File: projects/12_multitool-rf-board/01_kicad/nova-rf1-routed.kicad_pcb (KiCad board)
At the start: 4 copper layers, 110 x 66 mm, 87 parts, among them M1 vibro, SW1 RFswitch, SW2 RFswitch, U1 STM32WB55RG, U10 ESD, U2 CC1101, U3 ST25R3916, U5 ST7565R, U6 BQ25896, U7 BQ27220, U8 LM3281, U8B LM3281, U9 loadsw, X10 BAT+NTC, X6 FFC 18p, Y1 32MHz, Y2 32.768kHz

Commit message: proj12: rename board CRL-MT1 -> NOVA-RF1 (project-wide)
Global rename across source, docs, generated schematic/board/footprint-lib,
BOM/CPL, enclosure and fab tooling. No functional change. Footprint library
prefix crl-mt1: -> nova-rf1:; silkscreen/title/fab-file names updated.
(The in-flight compact route output will be renamed when it completes.)

Co-Authored-By: Claude Opus 4.8 <noreply@anthropic.com>
Claude-Session: https://claude.ai/code/session_01Hk6s8R6up8HYVQWXd3atVk
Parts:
- ANT1: footprint crl-mt1:Antenna_Chip -> nova-rf1:Antenna_Chip
- ANT_LF: footprint crl-mt1:RFID_125k_Coil -> nova-rf1:RFID_125k_Coil
- ANT_NFC: footprint crl-mt1:NFC_Loop_Antenna -> nova-rf1:NFC_Loop_Antenna
- BT1: footprint crl-mt1:Battery_3p -> nova-rf1:Battery_3p
- DA7: footprint crl-mt1:LP5562_DSBGA12 -> nova-rf1:LP5562_DSBGA12
- FLT1: footprint crl-mt1:RF_filter -> nova-rf1:RF_filter
- FLT2: footprint crl-mt1:Johanson_0310_Balun -> nova-rf1:Johanson_0310_Balun
- J_IBTN: footprint crl-mt1:iButton_Contacts -> nova-rf1:iButton_Contacts
- J_SD: footprint crl-mt1:microSD_7p -> nova-rf1:microSD_7p
- J_SWD: footprint crl-mt1:TagConnect_TC2030 -> nova-rf1:TagConnect_TC2030
- LS1: footprint crl-mt1:Speaker_2p -> nova-rf1:Speaker_2p
- M1: footprint crl-mt1:Vibro_2p -> nova-rf1:Vibro_2p
- SW1, SW2: footprint crl-mt1:RF_Switch_TSNP9 -> nova-rf1:RF_Switch_TSNP9
- U5: footprint crl-mt1:Display_ST7565_FFC -> nova-rf1:Display_ST7565_FFC
- U_IR: footprint crl-mt1:TSOP_IR_3p -> nova-rf1:TSOP_IR_3p
- VD4: footprint crl-mt1:LED_RGB_4p -> nova-rf1:LED_RGB_4p
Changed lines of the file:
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@@
 	(net 176 "unconnected-(U9-4)")
 	(net 177 "unconnected-(U9-5)")
-	(footprint "crl-mt1:TSOP_IR_3p"
+	(footprint "nova-rf1:TSOP_IR_3p"
 		(layer "F.Cu")
 		(at 66.065001 61.7751)
@@
 		(embedded_fonts no)
 	)
-	(footprint "crl-mt1:RF_Switch_TSNP9"
+	(footprint "nova-rf1:RF_Switch_TSNP9"
 		(layer "F.Cu")
 		(at 69.247619 71.9316)
@@
 		(embedded_fonts no)
 	)
-	(footprint "crl-mt1:Speaker_2p"
+	(footprint "nova-rf1:Speaker_2p"
 		(layer "F.Cu")
 		(at 99.617858 47.6786)
@@
 		(embedded_fonts no)
 	)
-	(footprint "crl-mt1:microSD_7p"
+	(footprint "nova-rf1:microSD_7p"
 		(layer "F.Cu")
 		(at 81.117858 47.2786)
@@
 		)
 	)
-	(footprint "crl-mt1:LP5562_DSBGA12"
+	(footprint "nova-rf1:LP5562_DSBGA12"
 		(layer "F.Cu")
 		(at 101.113334 71.088)
@@
 		)
 	)
-	(footprint "crl-mt1:LED_RGB_4p"
+	(footprint "nova-rf1:LED_RGB_4p"
 		(layer "F.Cu")
 		(at 82.466666 72.0316)
@@
 		)
 	)
-	(footprint "crl-mt1:Johanson_0310_Balun"
+	(footprint "nova-rf1:Johanson_0310_Balun"
 		(layer "F.Cu")
 		(at 106.117145 71.5316)
@@
 		(embedded_fonts no)
 	)
-	(footprint "crl-mt1:RF_filter"
+	(footprint "nova-rf1:RF_filter"
 		(layer "F.Cu")
 		(at 55.75 71.6316)
@@
 		(embedded_fonts no)
 	)
-	(footprint "crl-mt1:NFC_Loop_Antenna"
+	(footprint "nova-rf1:NFC_Loop_Antenna"
 		(locked yes)
 		(layer "F.Cu")
@@
 		(embedded_fonts no)
 	)
-	(footprint "crl-mt1:TagConnect_TC2030"
+	(footprint "nova-rf1:TagConnect_TC2030"
 		(locked yes)
 		(layer "F.Cu")
@@
 		)
 	)
-	(footprint "crl-mt1:iButton_Contacts"
+	(footprint "nova-rf1:iButton_Contacts"
 		(layer "F.Cu")
 		(at 90.367858 48.1786)
@@
 		)
 	)
-	(footprint "crl-mt1:Antenna_Chip"
+	(footprint "nova-rf1:Antenna_Chip"
 		(locked yes)
 		(layer "F.Cu")
@@
 		(embedded_fonts no)
 	)
-	(footprint "crl-mt1:Display_ST7565_FFC"
+	(footprint "nova-rf1:Display_ST7565_FFC"
 		(layer "F.Cu")
 		(at 57.675001 61.8751)
@@
 		)
 	)
-	(footprint "crl-mt1:RF_Switch_TSNP9"
+	(footprint "nova-rf1:RF_Switch_TSNP9"
 		(layer "F.Cu")
 		(at 75.866666 71.9316)
@@
 		)
 	)
-	(footprint "crl-mt1:RFID_125k_Coil"
+	(footprint "nova-rf1:RFID_125k_Coil"
 		(locked yes)
 		(layer "F.Cu")
@@
 		)
 	)
-	(footprint "crl-mt1:Vibro_2p"
+	(footprint "nova-rf1:Vibro_2p"
 		(layer "F.Cu")
 		(at 62.613096 72.6316)
@@
 		(embedded_fonts no)
 	)
-	(footprint "crl-mt1:Battery_3p"
+	(footprint "nova-rf1:Battery_3p"
 		(layer "F.Cu")
 		(at 90.574049 61.9751)

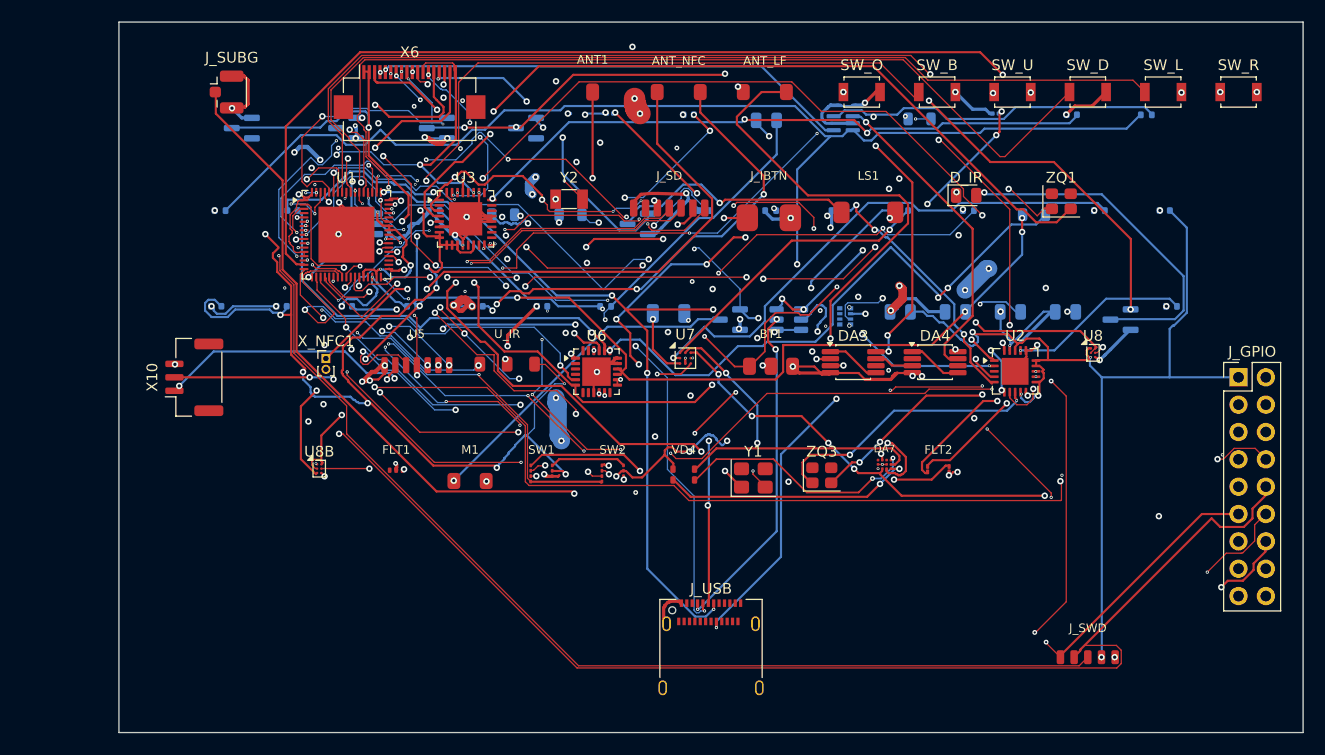
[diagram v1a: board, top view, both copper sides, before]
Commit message: proj12: NOVA-RF1 compact route 103/104 + both planes + full fab package
- +3V3 plane on In2.Cu (power nets closed), GND plane on In1.Cu
- 103/104 nets routed (NFC_CS needs 1 manual trace - only top+bottom free on a
  2-plane 4-layer board), 2965 segments, 530 vias; silkscreen added
- fab package: Gerber X2 + Excellon drill + map, CPL, JLCPCB + costed BOM
  (03_fab/NOVA-RF1_gerbers.zip etc.), names corrected in fab_export.sh
- refreshed routed-board render + product PDF; PCB_STATUS.md final section

Co-Authored-By: Claude Opus 4.8 <noreply@anthropic.com>
Claude-Session: https://claude.ai/code/session_01Hk6s8R6up8HYVQWXd3atVk
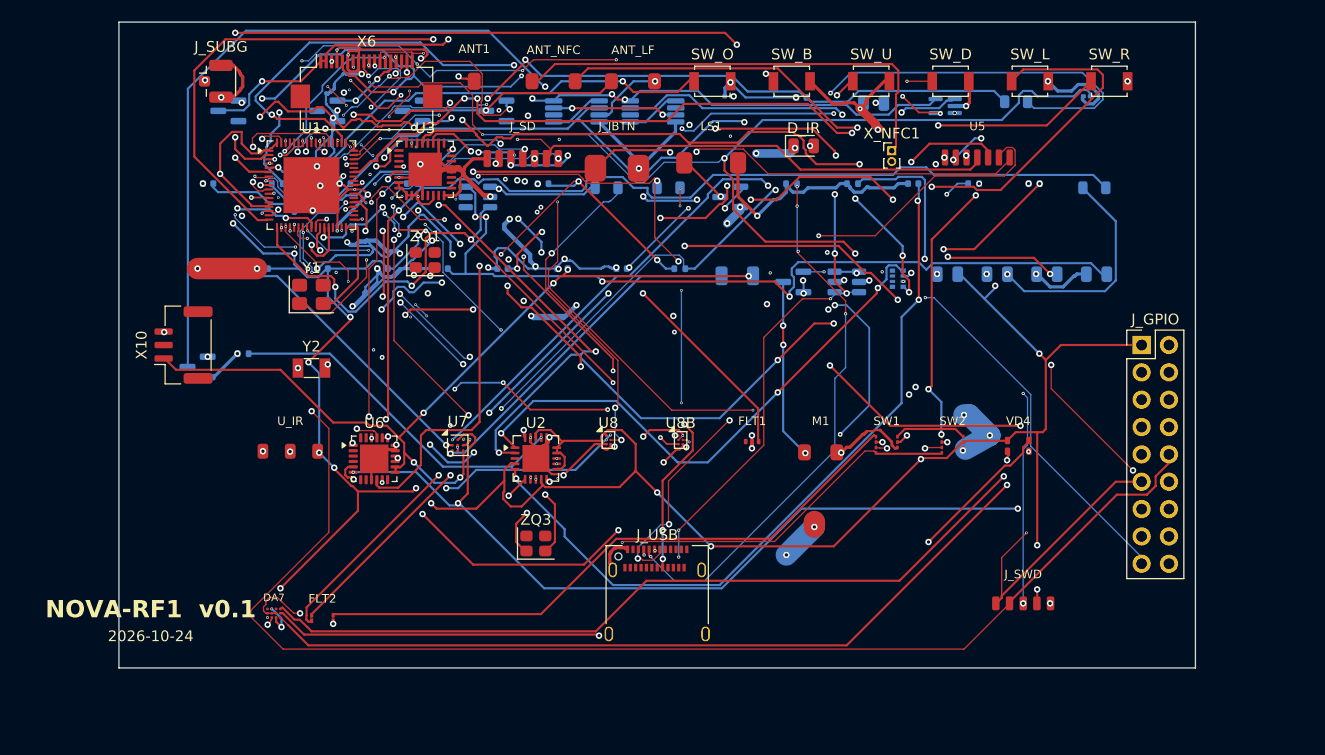
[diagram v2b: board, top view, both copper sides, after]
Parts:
- removed BT1: Li-Po 1S, nova-rf1:Battery_3p
- DA3, DA4: moved to B.Cu
- moved R13 86.3 mm to (41.5, 60.8)
- moved Q_IR 85.8 mm to (37.3, 62.0)
- moved C1 84.0 mm to (43.4, 52.9)
- moved R_FGB 83.5 mm to (37.8, 52.9)
- moved R_MID1 81.0 mm to (44.7, 45.0)
- moved C_AGDC 80.5 mm to (38.3, 45.0)
- moved ZQ1 59.3 mm to (58.4, 52.1)
- moved FLT2 58.9 mm to (48.9, 85.4)
- moved DA7 58.4 mm to (44.4, 84.9)
- moved X_NFC1 56.0 mm to (101.8, 42.0)
- moved U5 55.5 mm to (109.7, 42.6)
- moved U8 45.7 mm to (75.5, 68.8)
- moved U2 45.2 mm to (68.7, 70.5)
- moved Y1 44.5 mm to (47.9, 55.3)
- moved DA4 35.1 mm to (79.6, 38.3), turned to 180 degrees
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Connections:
- J_USB pad : unconnected-(J_USB-) -> (no net)
- U1 pad : unconnected-(U1-) -> (no net)
- U2 pad : unconnected-(U2-) -> (no net)
- U3 pad : unconnected-(U3-) -> (no net)
- U6 pad : unconnected-(U6-) -> (no net)
- VD_IBTN pad : unconnected-(VD_IBTN-) -> (no net)
- VD_USB pad : unconnected-(VD_USB-) -> (no net)
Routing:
- net GND: track 378.0 -> 460.5 mm, vias 97 -> 86
- net CC1101_GDO0: track 118.2 -> 38.2 mm, vias 4 -> 2
- net DISP_RST: track 12.8 -> 77.2 mm, vias 3 -> 5
- net BAT_NTC: track 64.2 -> 0.00 mm, vias 6 -> 0
- net CC1101_CS: track 105.1 -> 41.6 mm
- net NFC_XTAL2: track 75.6 -> 12.3 mm, vias 2 -> 4
- net DISP_DI: track 13.9 -> 75.7 mm, vias 3 -> 7
- net IR_LED_A: track 32.0 -> 90.2 mm, vias 1 -> 2
- net IR_TX: track 98.8 -> 41.6 mm, vias 5 -> 3
- net LED_G: track 21.3 -> 78.1 mm, vias 0 -> 2
- net LED_B: track 22.3 -> 77.2 mm
- net LED_R: track 23.5 -> 77.7 mm
- net NFC_XTAL1: track 72.3 -> 20.9 mm, vias 4 -> 3
- net CHG_ILIM: track 42.5 -> 88.1 mm, vias 3 -> 6
- net SUBG_ANT: track 62.7 -> 108.3 mm, vias 2 -> 4
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- added copper zone on In2.Cu, net +3V3
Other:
- board size 110 x 66 mm -> 100 x 60 mm
- board text added: "2026-10-24"
- board text added: "NOVA-RF1 v0.1"
- board text added: "Original firmware-compatible multi-tool - not a Flipper Zero"

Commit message: proj12: final elegant + corrected board routed 101/104 + fab package
Rounded handheld outline + the 3 verified netlist fixes. GND + +3V3 planes,
101/104 nets routed (3051 segs, 554 vias), silkscreen, Gerber/drill/CPL/BOM
re-exported, routed render + product PDF refreshed. 3 signals left for manual
trace (dense 2-plane 4-layer -> only top+bottom free); documented in PCB_STATUS.

Co-Authored-By: Claude Opus 4.8 <noreply@anthropic.com>
Claude-Session: https://claude.ai/code/session_01Hk6s8R6up8HYVQWXd3atVk
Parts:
- added C_A3V3: 1uF, Capacitor_SMD:C_0402_1005Metric, B.Cu at (44.7, 45.0)
- moved C10 83.9 mm to (37.3, 61.3)
- moved L_CHG 83.2 mm to (37.8, 53.3)
- moved R_CC2 6.33 mm to (104.5, 45.0)
- moved R_TS2 6.33 mm to (75.7, 45.0)
- moved C_BTST 6.33 mm to (63.6, 45.0)
- moved R_MID2 6.33 mm to (57.3, 45.0)
- moved C_CCd 6.33 mm to (110.1, 45.0)
- moved L13 6.33 mm to (81.6, 45.4)
- moved L14 6.33 mm to (87.4, 45.4)
- moved Q_SPK 6.33 mm to (93.1, 46.2)
- moved R_CC1 6.33 mm to (98.8, 45.0)
- moved R_FGO 6.33 mm to (115.7, 45.0)
- moved R_ILIM 6.33 mm to (121.3, 45.0)
- moved R_MID1 6.33 mm to (51.0, 45.0)
- moved U9 6.33 mm to (69.7, 46.2)
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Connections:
- DA8 pad 2: +3V3_LDO -> A3V3
- VT4 pad 2: +5V -> VSYS
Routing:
- net +3V3: track 297.7 -> 164.8 mm, vias 28 -> 45
- net USB_DP: track 120.2 -> 46.2 mm, vias 11 -> 4
- net VIBRO: track 146.6 -> 96.9 mm, vias 13 -> 7
- net CHG_SW: track 93.6 -> 45.7 mm, vias 3 -> 4
- net GND: track 460.5 -> 504.0 mm, vias 86 -> 118
- net RFID_CARRIER: track 63.5 -> 31.2 mm, vias 3 -> 5
- net NFC_CS: track 80.5 -> 112.3 mm, vias 7 -> 5
- net +3V3_PERIPH: track 75.9 -> 44.7 mm, vias 4 -> 5
- net SPI_R_SCK: track 118.7 -> 146.1 mm, vias 12 -> 11
- net I2C_PWR_SCL: track 130.5 -> 103.3 mm, vias 8 -> 4
- net IR_LED_A: track 90.2 -> 64.1 mm, vias 2 -> 7
- net A3V3: track 75.7 -> 99.7 mm, vias 4 -> 9
- net I2C_PWR_SDA: track 151.9 -> 128.6 mm
- net RFID_RF_IN: track 99.0 -> 79.4 mm, vias 9 -> 6
- net EXT_PC3: track 108.3 -> 89.1 mm
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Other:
- outline, holes or cut-outs redrawn
